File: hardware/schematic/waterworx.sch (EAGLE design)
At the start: 104 parts, among them J2 POWER_JACKPTH, Q1 8MHz, Q2 32.768 KHz, T1 LF-TRIACSOT223, T10 LF-TRIACSOT223, T15 LF-TRIACSOT223, T16 LF-TRIACSOT223, T2 LF-TRIACSOT223, T3 LF-TRIACSOT223, T4 LF-TRIACSOT223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

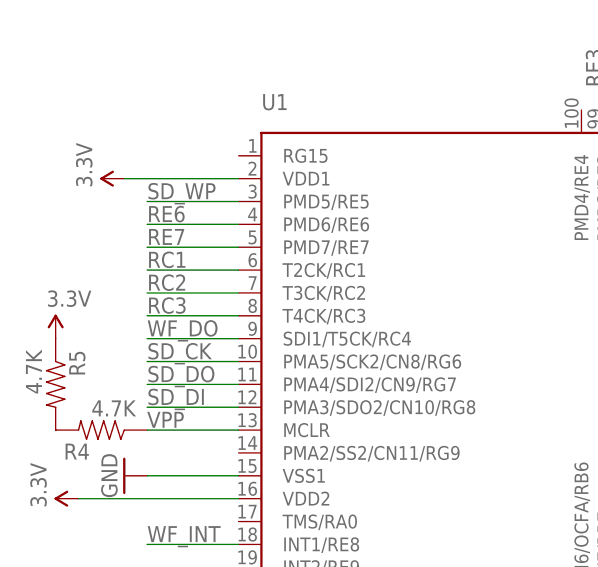
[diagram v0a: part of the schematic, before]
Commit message: Remove unused nets from waterworx.sch. Added triac test board and new dev board stub.
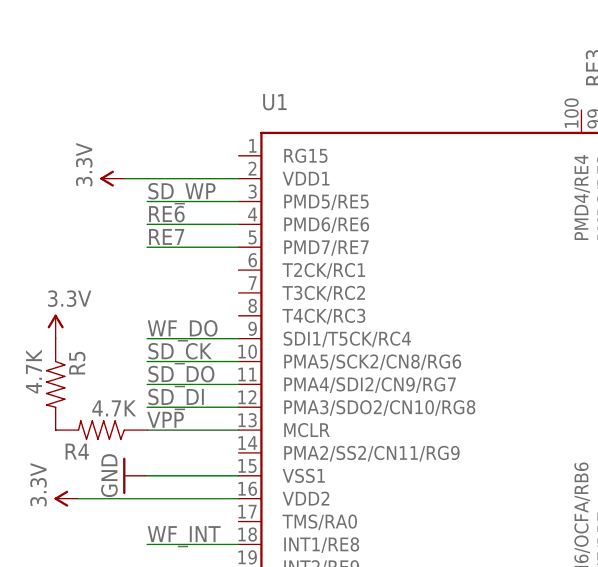
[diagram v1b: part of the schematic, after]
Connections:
- removed net RC1: U1.T2CK/RC1
- removed net RC2: U1.T3CK/RC2
- removed net RC3: U1.T4CK/RC3
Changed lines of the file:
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@@
-</segment>
-</net>
-<net name="RC1" class="0">
-<segment>
-<wire x1="30.48" y1="81.28" x2="20.32" y2="81.28" width="0.1524" layer="91"/>
-<label x="20.32" y="81.534" size="1.778" layer="95"/>
-<pinref part="U1" gate="G$1" pin="T2CK/RC1"/>
-</segment>
-</net>
-<net name="RC2" class="0">
-<segment>
-<wire x1="30.48" y1="78.74" x2="20.32" y2="78.74" width="0.1524" layer="91"/>
-<label x="20.32" y="78.994" size="1.778" layer="95"/>
-<pinref part="U1" gate="G$1" pin="T3CK/RC2"/>
-</segment>
-</net>
-<net name="RC3" class="0">
-<segment>
-<wire x1="30.48" y1="76.2" x2="20.32" y2="76.2" width="0.1524" layer="91"/>
-<label x="20.32" y="76.454" size="1.778" layer="95"/>
-<pinref part="U1" gate="G$1" pin="T4CK/RC3"/>
 </segment>
 </net>

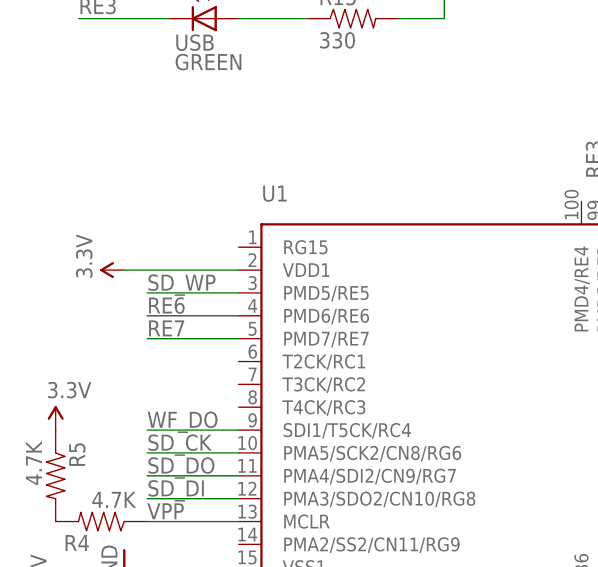
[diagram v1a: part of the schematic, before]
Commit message: First revision of dev board.  Fixed duplicate pin in waterworx.sch
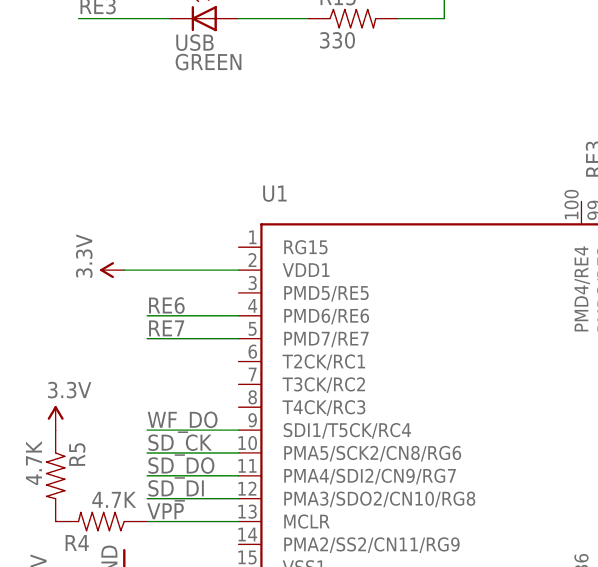
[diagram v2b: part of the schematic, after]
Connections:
- net SD_WP: no longer U1.PMD5/RE5
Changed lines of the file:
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@@
 <net name="SD_WP" class="0">
 <segment>
-<wire x1="30.48" y1="88.9" x2="20.32" y2="88.9" width="0.1524" layer="91"/>
-<label x="20.32" y="89.154" size="1.778" layer="95"/>
-<pinref part="U1" gate="G$1" pin="PMD5/RE5"/>
 <wire x1="190.5" y1="231.14" x2="180.34" y2="231.14" width="0.1524" layer="91"/>
 <label x="182.88" y="231.394" size="1.778" layer="95"/>

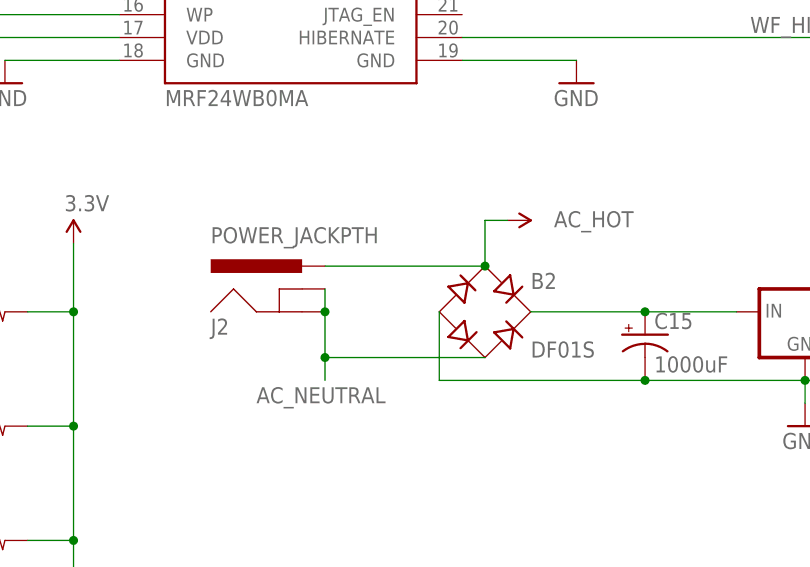
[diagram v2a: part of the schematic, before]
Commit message: Added fuse holder to lib.  Swapped 10k res for 2 4.7K in dev board.  Added fuse to waterworx.sch
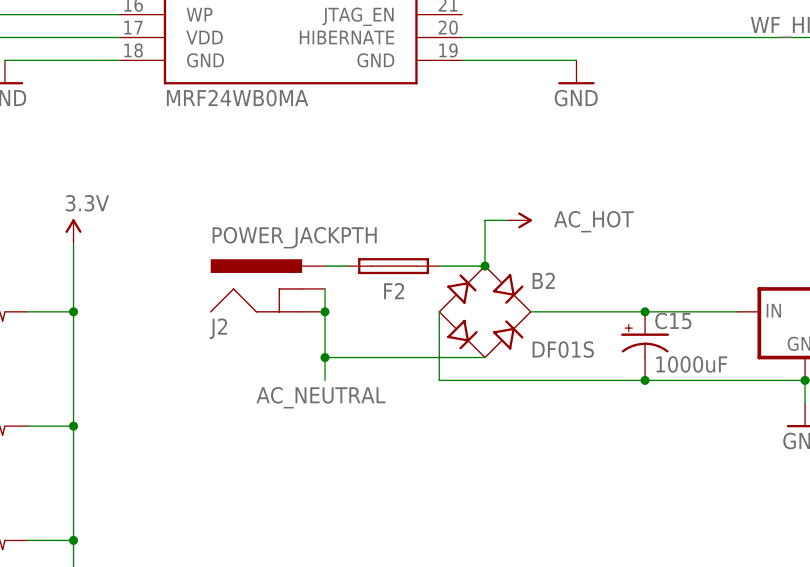
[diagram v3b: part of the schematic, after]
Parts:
- added F2: (no value), lizardworx:LITTLEFUSENANO
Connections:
- new net N$37: F2.1, J2.PWR
- net AC_HOT: now also F2.2; no longer J2.PWR
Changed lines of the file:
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@@
 <part name="GND4" library="SparkFun02-20-08" deviceset="GND" device=""/>
 <part name="U$3" library="lizardworx" deviceset="VNEG" device="" value="AC_HOT"/>
+<part name="F2" library="lizardworx" deviceset="LITTLEFUSE" device="NANO"/>
 </parts>
 <sheets>
@@
 <instance part="GND4" gate="1" x="332.74" y="91.44"/>
 <instance part="U$3" gate="G$2" x="368.3" y="111.76" rot="R180"/>
+<instance part="F2" gate="A" x="88.9" y="162.56" smashed="yes">
+<attribute name="NAME" x="87.63" y="158.877" size="1.778" layer="95"/>
+<attribute name="VALUE" x="85.09" y="159.639" size="1.778" layer="96"/>
+</instance>
 </instances>
 <busses>
@@
 </segment>
 <segment>
-<pinref part="J2" gate="G$1" pin="PWR"/>
-<wire x1="81.28" y1="162.56" x2="99.06" y2="162.56" width="0.1524" layer="91"/>
 <pinref part="B2" gate="G$1" pin="AC1"/>
 <wire x1="99.06" y1="162.56" x2="99.06" y2="167.64" width="0.1524" layer="91"/>
-<junction x="99.06" y="162.56"/>
 <wire x1="99.06" y1="167.64" x2="101.6" y2="167.64" width="0.1524" layer="91"/>
 <pinref part="U$4" gate="G$2" pin="P$1"/>
+<pinref part="F2" gate="A" pin="2"/>
+<wire x1="93.98" y1="162.56" x2="99.06" y2="162.56" width="0.1524" layer="91"/>
+<junction x="99.06" y="162.56"/>
 </segment>
 <segment>
@@
 </segment>
 </net>
+<net name="N$37" class="0">
+<segment>
+<pinref part="J2" gate="G$1" pin="PWR"/>
+<pinref part="F2" gate="A" pin="1"/>
+<wire x1="83.82" y1="162.56" x2="81.28" y2="162.56" width="0.1524" layer="91"/>
+</segment>
+</net>

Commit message: First prototype version of board complete
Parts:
- added R31, R32: 4.7K, SparkFun-Passives:RESISTOR0603-RES
- S1: value (none) -> S1
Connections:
- net 3.3V: now also R31.1, R32.1
- net SD_CD: now also R32.2
- net SD_WP: now also R31.2
- net STATION_1: now also JP2.1; no longer JP2.4
- net STATION_10: now also JP4.2; no longer JP4.3
- net STATION_11: now also JP4.3; no longer JP4.2
- net STATION_12: now also JP4.4; no longer JP4.1
- net STATION_2: now also JP2.2; no longer JP2.3
- net STATION_3: now also JP2.3; no longer JP2.2
- net STATION_4: now also JP2.4; no longer JP2.1
- net STATION_5: now also JP3.1; no longer JP3.4
- net STATION_6: now also JP3.2; no longer JP3.3
- net STATION_7: now also JP3.3; no longer JP3.2
- net STATION_8: now also JP3.4; no longer JP3.1
- net STATION_9: now also JP4.1; no longer JP4.4
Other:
- moved on the sheet: J2, JP2, JP3, JP4
